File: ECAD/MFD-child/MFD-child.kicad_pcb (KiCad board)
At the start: 2 copper layers, 136.2 x 158.7 mm, 44 parts, among them J1 ICSP, J2 Conn_01x05, J3 Conn_01x05, SW1 RESET, SW11 OSB1, SW12 OSB2, SW13 OSB3, SW14 OSB4, SW15 OSB5, SW16 SYM-UP, SW17 SYM-DN, SW2 SW_Coded_SH-7010, SW21 OSB6, SW22 OSB7, SW23 OSB8, SW24 OSB9, SW25 OSB10, SW26 CON-UP, SW27 CON-DN, SW31 OSB11, SW32 OSB12, SW33 OSB13, SW34 OSB14, SW35 OSB15, SW36 BRT-UP, SW37 BRT-DN, SW41 OSB16, SW42 OSB17, SW43 OSB18, SW44 OSB19, SW45 OSB20, SW46 GAIN-UP, SW47 GAIN-DN

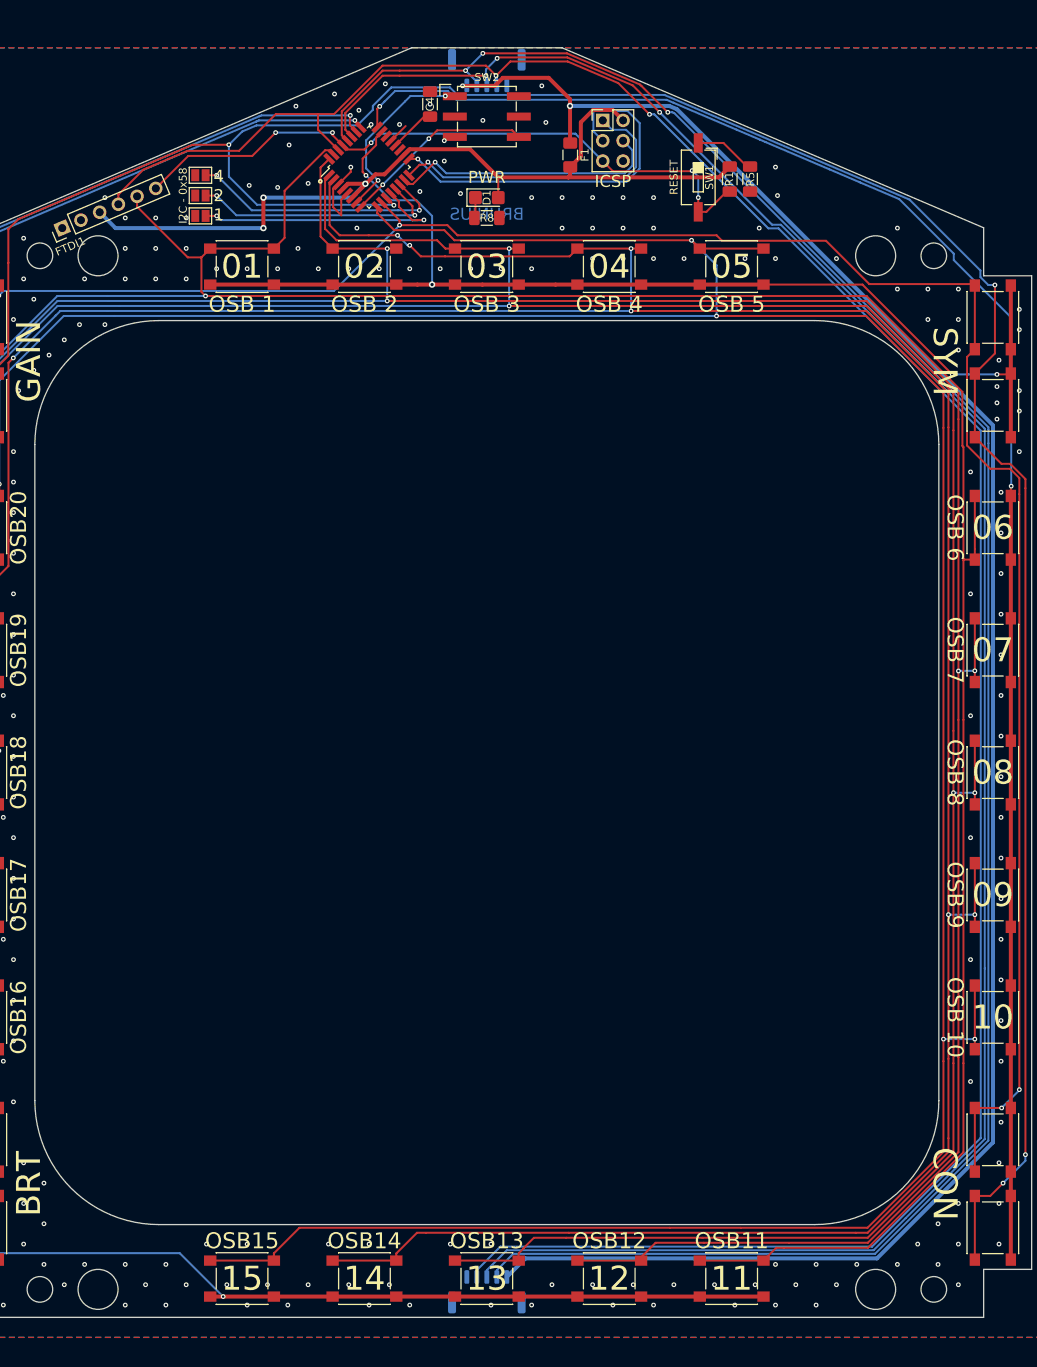
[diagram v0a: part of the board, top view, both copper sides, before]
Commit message: Swap bus connector to 4-pin JST-GH
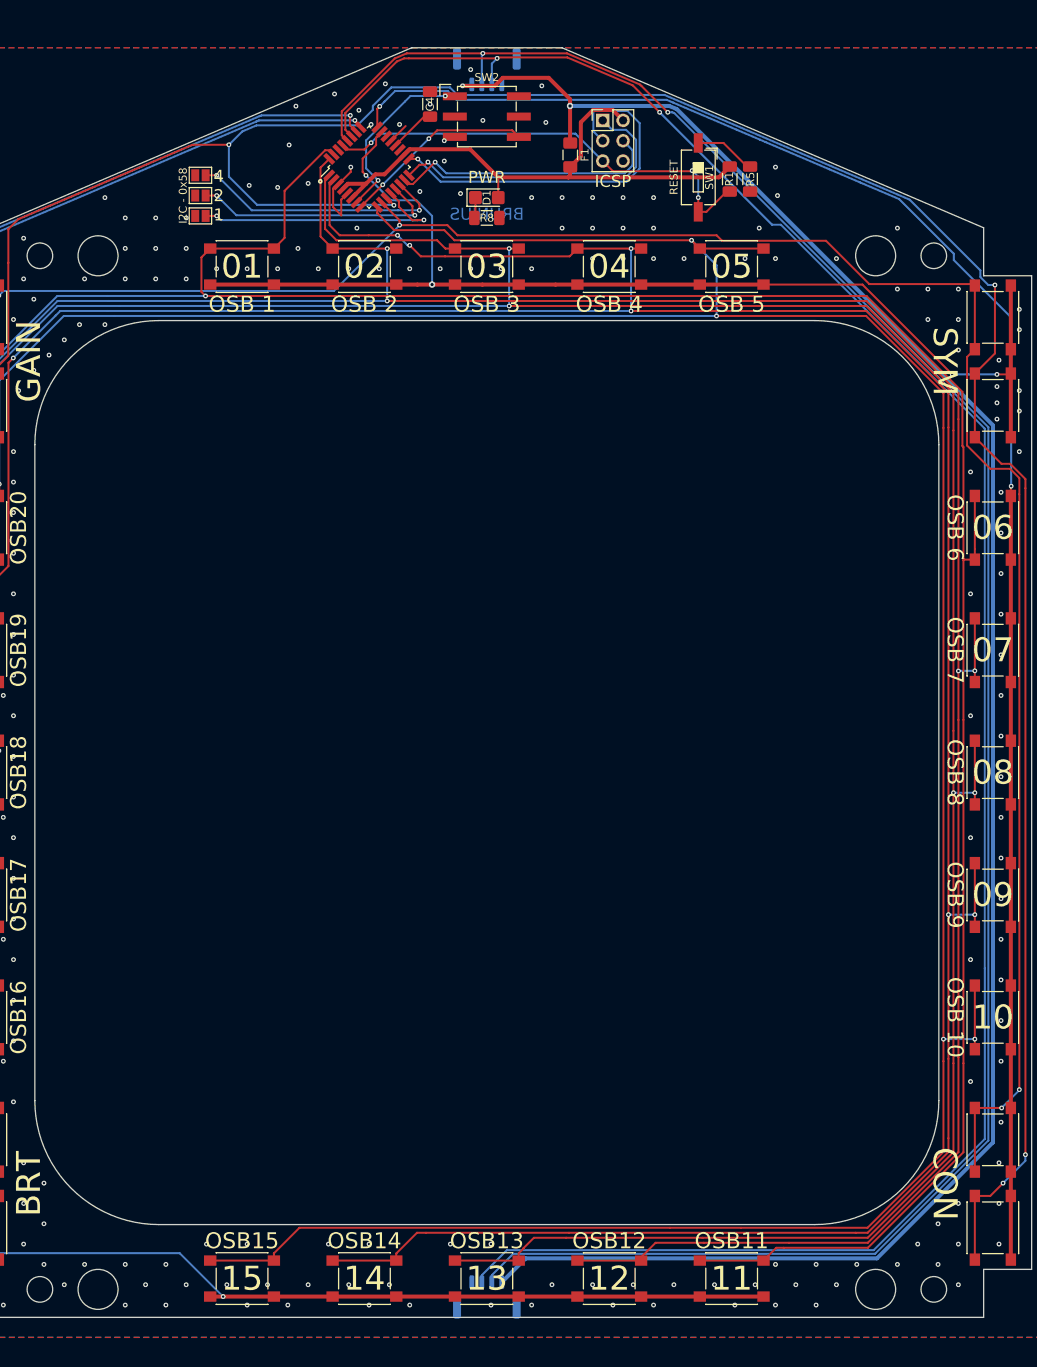
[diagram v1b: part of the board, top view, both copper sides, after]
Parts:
- removed FTDI1: Conn_01x06, Connector_PinHeader_2.54mm:PinHeader_1x06_P2.54mm_Vertical
- J2, J3: value Conn_01x05 -> Conn_01x04; footprint Connector_JST:JST_GH_SM05B-GHS-TB_1x05-1MP_P1.25mm_Horizontal -> Connector_JST:JST_GH_SM04B-GHS-TB_1x04-1MP_P1.25mm_Horizontal
- moved J3 0.64 mm to (70.6, 136.1)
- moved J2 0.13 mm to (70.6, -17.3)
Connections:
- J2 pad 4: BUS_SIGNAL -> GNDREF
- J3 pad 4: BUS_SIGNAL -> GNDREF
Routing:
- net BUS_SIGNAL: track 301.6 -> 0.00 mm, vias 2 -> 0
- net +5V: track 109.9 -> 71.3 mm, vias 3 -> 0
- net RESET: track 83.9 -> 56.8 mm, vias 5 -> 3
- net R1: track 403.4 -> 391.5 mm
- net SDA: track 265.0 -> 267.6 mm, vias 3 -> 2
- net SCL: track 266.9 -> 269.2 mm, vias 3 -> 2
- net Net-(F1-Pad1): track 247.8 -> 249.4 mm
- net GNDREF: vias 195 -> 196
